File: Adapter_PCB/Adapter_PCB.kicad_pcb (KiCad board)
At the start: 2 copper layers, 40 x 21 mm, 3 parts, among them J1 Conn_01x10, J2 USB_B_Micro, J3 Conn_01x06

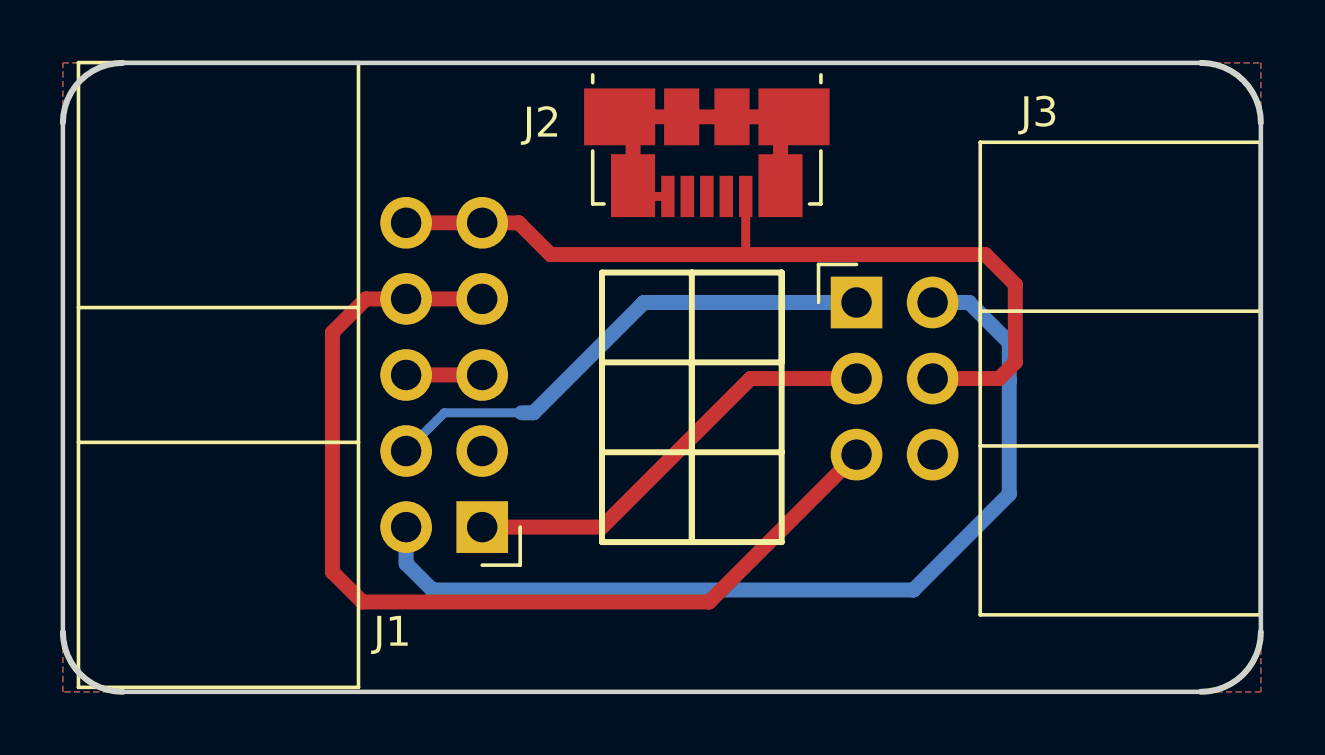
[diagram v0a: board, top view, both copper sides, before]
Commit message: Add 4 pin connector, change connector pinout, add silkscreen
Only one of reducing connectors can be populated.
In silkscreen are now connector pinouts diagrams and logo with QR code.
Connector pinout was rearranged to mach IDC cable with lock on different sides.
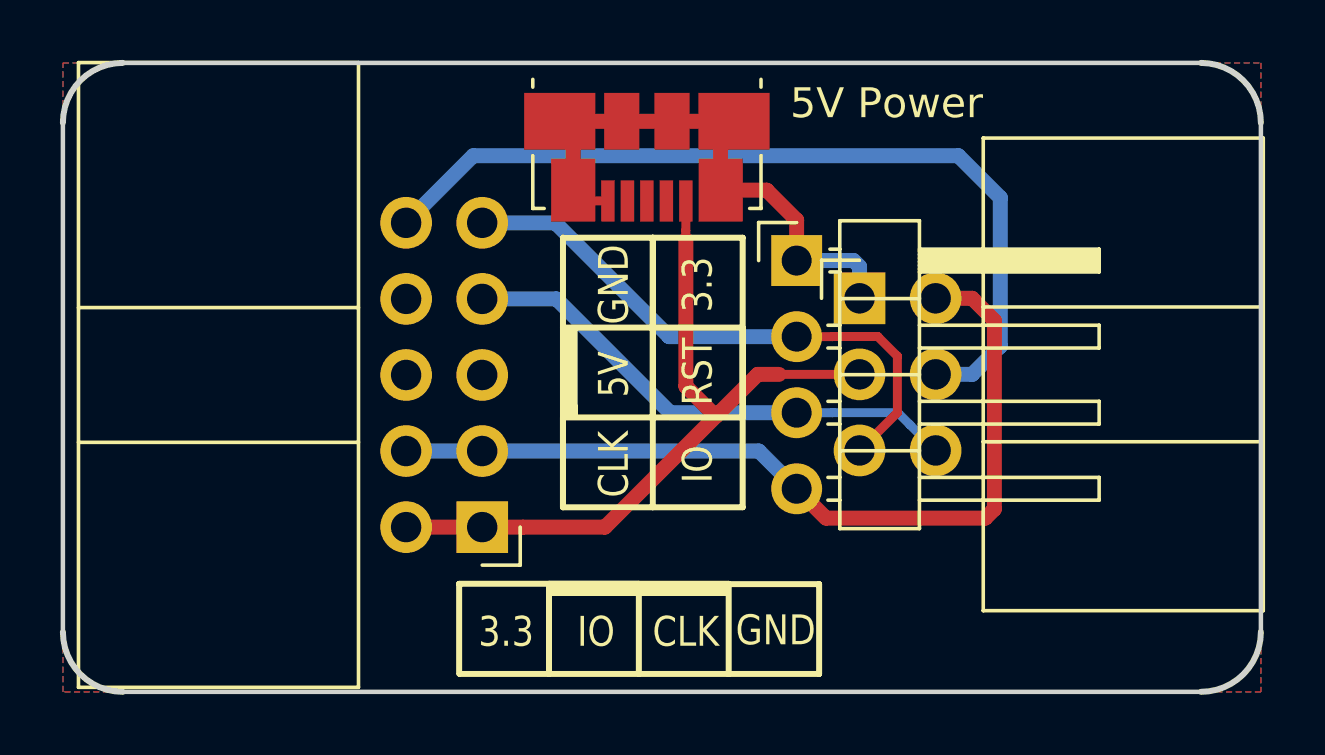
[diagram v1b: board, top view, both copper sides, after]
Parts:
- added G***: LOGO, TCY_logo:TCY_LOGO_13x6mm, B.Cu at (165.2, 97.5)
- added G***: LOGO, TCY_logo:#QR_ST-Link_adapter, B.Cu at (180.9, 97.4)
- added J4: Conn_01x04, Connector_PinHeader_2.54mm:PinHeader_1x04_P2.54mm_Horizontal, F.Cu at (170.5, 93.6)
- moved J2 2.01 mm to (165.5, 90.2)
- moved J3 0.17 mm to (172.6, 94.9)
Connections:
- J1 pad 2: Net-(J1-Pad2) -> Net-(J1-Pad1)
- J1 pad 4: Net-(J1-Pad4) -> Net-(J1-Pad3)
- J1 pad 8: Net-(J1-Pad7) -> Net-(J1-Pad8)
- J1 pad 9: Net-(J1-Pad10) -> Net-(J1-Pad9)
- J2 pad 1: Net-(J1-Pad10) -> Net-(J1-Pad1)
- J3 pad 1: Net-(J1-Pad4) -> GND
- J3 pad 2: Net-(J1-Pad2) -> Net-(J1-Pad3)
- J3 pad 5: Net-(J1-Pad7) -> Net-(J1-Pad9)
- J3 pad 6: GND -> Net-(J1-Pad7)
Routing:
- net Net-(J1-Pad2): track 31.2 -> 0.00 mm
- net Net-(J1-Pad3): track 0.00 -> 29.3 mm
- net Net-(J1-Pad9): track 0.00 -> 19.4 mm
- net Net-(J1-Pad4): track 17.1 -> 0.00 mm
- net Net-(J1-Pad7): track 33.4 -> 17.2 mm
- net Net-(J1-Pad1): track 14.6 -> 26.2 mm
- net GND: track 14.6 -> 19.6 mm
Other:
- board text added: "3.3"
- board text added: "5V"
- board text added: "5V Power"
- board text added: "CLK"
- board text added: "GND"
- board text added: "IO"
- board text added: "RST"
- board text added: "SW IM"

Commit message: Update PCB, change QR to match correct repository address
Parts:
- moved G*** 0.07 mm to (180.9, 97.5)
